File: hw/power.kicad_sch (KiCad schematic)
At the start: 48 parts, among them J9 Expansion, Q8 DMC2053UVT, U1 RT8096B, U2 RT8096B, U3 RT8096B, U5 TPS563249DDC

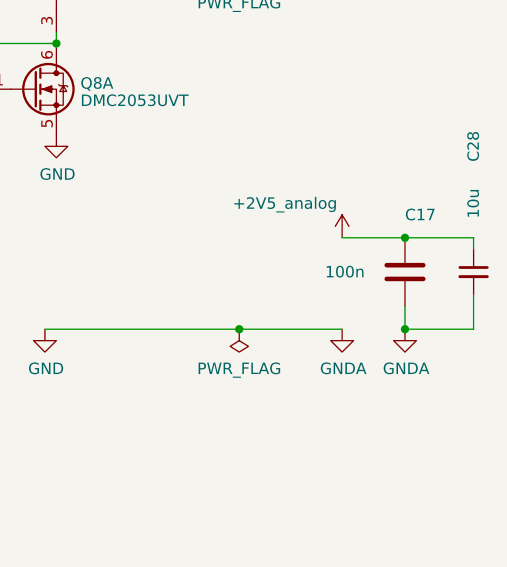
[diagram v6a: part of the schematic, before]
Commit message: consolidated components to simplify BOM
(nothing actually changed but the symbols representing identical
components are now identical -> no more multiple BOM entries for
the same type of component).
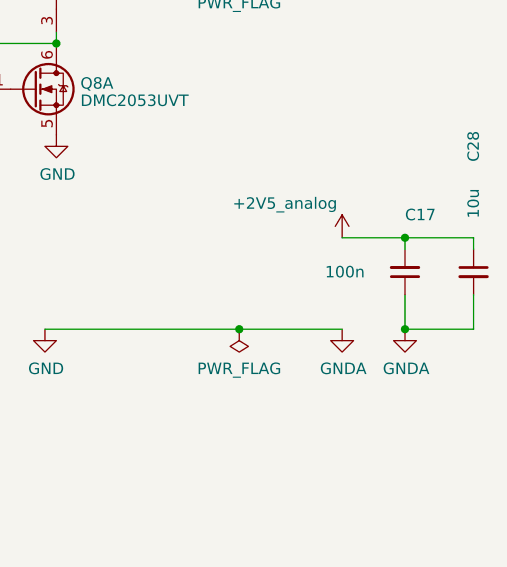
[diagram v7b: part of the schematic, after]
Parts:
- C1, C11, C12, C15, C16, C2, C28, C3, C31, C57, C7, C8: Manufacturer (none) -> Samsung; Part (none) -> CL31A106KPHNNNE
- C10, C13: Manufacturer (none) -> Samsung; Part (none) -> CL10B104KB8NFN
- C17: symbol fmc:100nF_603 -> Device:C_Small; Manufacturer (none) -> Samsung; Part (none) -> CL10B104KB8NFN
- C4: Manufacturer Wurth -> (none); Part 885012006050 -> (none)
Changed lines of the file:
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@@
     (stroke (width 0) (type default))
   )
-  (wire (pts (xy 259.715 96.52) (xy 259.715 99.06))
+  (wire (pts (xy 259.715 95.25) (xy 259.715 99.06))
     (stroke (width 0) (type default))
   )
@@
   )
   (wire (pts (xy 189.23 129.54) (xy 189.23 119.38))
+    (stroke (width 0) (type default))
+  )
+  (wire (pts (xy 259.715 88.9) (xy 259.715 90.17))
     (stroke (width 0) (type default))
   )
@@
       (effects (font (size 1.27 1.27)) hide)
     )
-    (property "Part" "" (at 54.61 72.39 0)
-      (effects (font (size 1.27 1.27)) hide)
-    )
-    (property "Manufacturer" "" (at 54.61 72.39 0)
+    (property "Part" "CL31A106KPHNNNE" (at 54.61 72.39 0)
+      (effects (font (size 1.27 1.27)) hide)
+    )
+    (property "Manufacturer" "Samsung" (at 54.61 72.39 0)
       (effects (font (size 1.27 1.27)) hide)
     )
@@
       (effects (font (size 1.27 1.27)) hide)
     )
-    (property "Part" "" (at 99.06 74.93 0)
-      (effects (font (size 1.27 1.27)) hide)
-    )
-    (property "Manufacturer" "" (at 99.06 74.93 0)
+    (property "Part" "CL31A106KPHNNNE" (at 99.06 74.93 0)
+      (effects (font (size 1.27 1.27)) hide)
+    )
+    (property "Manufacturer" "Samsung" (at 99.06 74.93 0)
       (effects (font (size 1.27 1.27)) hide)
     )
@@
       (effects (font (size 1.27 1.27)) hide)
     )
-    (property "Part" "885012006050" (at 90.17 76.2 90)
-      (effects (font (size 1.27 1.27)) hide)
-    )
-    (property "Manufacturer" "Wurth" (at 90.17 76.2 90)
+    (property "Part" "" (at 90.17 76.2 90)
+      (effects (font (size 1.27 1.27)) hide)
+    )
+    (property "Manufacturer" "" (at 90.17 76.2 90)
       (effects (font (size 1.27 1.27)) hide)
     )
@@
       (effects (font (size 1.27 1.27)) hide)
     )
-    (property "Part" "" (at 54.61 109.22 0)
-      (effects (font (size 1.27 1.27)) hide)
-    )
-    (property "Manufacturer" "" (at 54.61 109.22 0)
+    (property "Part" "CL31A106KPHNNNE" (at 54.61 109.22 0)
+      (effects (font (size 1.27 1.27)) hide)
+    )
+    (property "Manufacturer" "Samsung" (at 54.61 109.22 0)
       (effects (font (size 1.27 1.27)) hide)
     )
@@
       (effects (font (size 1.27 1.27)) hide)
     )
-    (property "Part" "" (at 99.06 111.76 0)
-      (effects (font (size 1.27 1.27)) hide)
-    )
-    (property "Manufacturer" "" (at 99.06 111.76 0)
+    (property "Part" "CL31A106KPHNNNE" (at 99.06 111.76 0)
+      (effects (font (size 1.27 1.27)) hide)
+    )
+    (property "Manufacturer" "Samsung" (at 99.06 111.76 0)
       (effects (font (size 1.27 1.27)) hide)
     )
@@
       (effects (font (size 1.27 1.27)) hide)
     )
-    (property "Part" "" (at 54.61 34.29 0)
-      (effects (font (size 1.27 1.27)) hide)
-    )
-    (property "Manufacturer" "" (at 54.61 34.29 0)
+    (property "Part" "CL31A106KPHNNNE" (at 54.61 34.29 0)
+      (effects (font (size 1.27 1.27)) hide)
+    )
+    (property "Manufacturer" "Samsung" (at 54.61 34.29 0)
       (effects (font (size 1.27 1.27)) hide)
     )
@@
       (effects (font (size 1.27 1.27)) hide)
     )
-    (property "Part" "" (at 99.06 36.83 0)
-      (effects (font (size 1.27 1.27)) hide)
-    )
-    (property "Manufacturer" "" (at 99.06 36.83 0)
+    (property "Part" "CL31A106KPHNNNE" (at 99.06 36.83 0)
+      (effects (font (size 1.27 1.27)) hide)
+    )
+    (property "Manufacturer" "Samsung" (at 99.06 36.83 0)
       (effects (font (size 1.27 1.27)) hide)
     )
@@
       (effects (font (size 1.27 1.27)) hide)
     )
+    (property "Manufacturer" "Samsung" (at 66.04 140.97 0)
+      (effects (font (size 1.27 1.27)) hide)
+    )
+    (property "Part" "CL31A106KPHNNNE" (at 66.04 140.97 0)
+      (effects (font (size 1.27 1.27)) hide)
+    )
     (pin "1")
     (pin "2")
@@
       (effects (font (size 1.27 1.27)) hide)
     )
+    (property "Manufacturer" "Samsung" (at 267.335 92.71 0)
+      (effects (font (size 1.27 1.27)) hide)
+    )
+    (property "Part" "CL31A106KPHNNNE" (at 267.335 92.71 0)
+      (effects (font (size 1.27 1.27)) hide)
+    )
     (pin "1")
     (pin "2")
@@
     )
   )
-  (symbol (lib_id "fmc:100nF_603") (at 259.715 92.71 180) (unit 1)
+  (symbol (lib_id "Device:C_Small") (at 259.715 92.71 180) (unit 1)
     (in_bom yes) (on_board yes) (dnp no)
     (property "Reference" "C17" (at 259.715 86.36 0)
@@
       (effects (font (size 1.27 1.27)) (justify right))
     )
-    (property "Footprint" "Capacitor_SMD:C_0603_1608Metric" (at 258.7498 88.9 0)
+    (property "Footprint" "Capacitor_SMD:C_0603_1608Metric" (at 259.715 92.71 0)
       (effects (font (size 1.27 1.27)) hide)
     )
@@
       (effects (font (size 1.27 1.27)) hide)
     )
-    (property "Part" "" (at 256.54 97.79 0)
-      (effects (font (size 1.27 1.27)) hide)
-    )
-    (property "Manufacturer" "" (at 254 100.33 0)
+    (property "Part" "CL10B104KB8NFN" (at 256.54 97.79 0)
+      (effects (font (size 1.27 1.27)) hide)
+    )
+    (property "Manufacturer" "Samsung" (at 254 100.33 0)
       (effects (font (size 1.27 1.27)) hide)
     )
@@
       (effects (font (size 1.27 1.27)) hide)
     )
+    (property "Manufacturer" "Samsung" (at 57.15 140.97 0)
+      (effects (font (size 1.27 1.27)) hide)
+    )
+    (property "Part" "CL10B104KB8NFN" (at 57.15 140.97 0)
+      (effects (font (size 1.27 1.27)) hide)
+    )
     (pin "1")
     (pin "2")
@@
       (effects (font (size 1.27 1.27)) hide)
     )
+    (property "Manufacturer" "Samsung" (at 128.27 140.97 0)
+      (effects (font (size 1.27 1.27)) hide)
+    )
+    (property "Part" "CL31A106KPHNNNE" (at 128.27 140.97 0)
+      (effects (font (size 1.27 1.27)) hide)
+    )
     (pin "1")
     (pin "2")
@@
       (effects (font (size 1.27 1.27)) hide)
     )
+    (property "Manufacturer" "Samsung" (at 71.12 140.97 0)
+      (effects (font (size 1.27 1.27)) hide)
+    )
+    (property "Part" "CL31A106KPHNNNE" (at 71.12 140.97 0)
+      (effects (font (size 1.27 1.27)) hide)
+    )
     (pin "1")
     (pin "2")
@@
       (effects (font (size 1.27 1.27)) hide)
     )
+    (property "Manufacturer" "Samsung" (at 133.35 140.97 0)
+      (effects (font (size 1.27 1.27)) hide)
+    )
+    (property "Part" "CL31A106KPHNNNE" (at 133.35 140.97 0)
+      (effects (font (size 1.27 1.27)) hide)
+    )
     (pin "1")
     (pin "2")
@@
       (effects (font (size 1.27 1.27)) hide)
     )
-    (property "Part" "" (at 104.14 36.83 0)
-      (effects (font (size 1.27 1.27)) hide)
-    )
-    (property "Manufacturer" "" (at 104.14 36.83 0)
+    (property "Part" "CL31A106KPHNNNE" (at 104.14 36.83 0)
+      (effects (font (size 1.27 1.27)) hide)
+    )
+    (property "Manufacturer" "Samsung" (at 104.14 36.83 0)
       (effects (font (size 1.27 1.27)) hide)
     )
@@
       (effects (font (size 1.27 1.27)) hide)
     )
+    (property "Manufacturer" "Samsung" (at 102.87 140.97 0)
+      (effects (font (size 1.27 1.27)) hide)
+    )
+    (property "Part" "CL10B104KB8NFN" (at 102.87 140.97 0)
+      (effects (font (size 1.27 1.27)) hide)
+    )

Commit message: consolidated ferrite beads (use same everywhere)
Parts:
- FB1, FB3, FB5: value Ferrite_Bead MPZ1608S221A -> 600Ohm@100MHz; Manufacturer TDK -> Laird; Part MPZ1608S221ATA00 -> MI0603J601R-10
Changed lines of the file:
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@@
       (effects (font (size 1.27 1.27)))
     )
-    (property "Value" "Ferrite_Bead MPZ1608S221A" (at 111.76 171.45 90)
+    (property "Value" "600Ohm@100MHz" (at 111.76 171.45 90)
       (effects (font (size 1.27 1.27)) hide)
     )
@@
       (effects (font (size 1.27 1.27)) hide)
     )
-    (property "Part" "MPZ1608S221ATA00" (at 111.76 165.1 90)
+    (property "Part" "MI0603J601R-10" (at 111.76 165.1 90)
       (effects (font (size 1.27 1.27)) hide)
     )
-    (property "Manufacturer" "TDK" (at 111.76 165.1 90)
+    (property "Manufacturer" "Laird" (at 111.76 165.1 90)
       (effects (font (size 1.27 1.27)) hide)
     )
@@
       (effects (font (size 1.27 1.27)))
     )
-    (property "Value" "Ferrite_Bead MPZ1608S221A" (at 233.68 64.77 90)
+    (property "Value" "600Ohm@100MHz" (at 233.68 64.77 90)
       (effects (font (size 1.27 1.27)) hide)
     )
@@
       (effects (font (size 1.27 1.27)) hide)
     )
-    (property "Part" "MPZ1608S221ATA00" (at 233.68 58.42 90)
+    (property "Part" "MI0603J601R-10" (at 233.68 58.42 90)
       (effects (font (size 1.27 1.27)) hide)
     )
-    (property "Manufacturer" "TDK" (at 233.68 58.42 90)
+    (property "Manufacturer" "Laird" (at 233.68 58.42 90)
       (effects (font (size 1.27 1.27)) hide)
     )
@@
       (effects (font (size 1.27 1.27)))
     )
-    (property "Value" "Ferrite_Bead MPZ1608S221A" (at 111.76 113.03 90)
+    (property "Value" "600Ohm@100MHz" (at 111.76 113.03 90)
       (effects (font (size 1.27 1.27)) hide)
     )
@@
       (effects (font (size 1.27 1.27)) hide)
     )
-    (property "Part" "MPZ1608S221ATA00" (at 111.76 106.68 90)
+    (property "Part" "MI0603J601R-10" (at 111.76 106.68 90)
       (effects (font (size 1.27 1.27)) hide)
     )
-    (property "Manufacturer" "TDK" (at 111.76 106.68 90)
+    (property "Manufacturer" "Laird" (at 111.76 106.68 90)
       (effects (font (size 1.27 1.27)) hide)
     )
